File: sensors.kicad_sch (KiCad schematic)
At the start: 55 parts, among them IC1 TCA9548ARGERQ1, IC2 SGP40-D-R4, IC3 SGP40-D-R4, IC4 SGP40-D-R4, IC6 SGP40-D-R4, U3 BMP581, U4 BMP581, U5 BMP581, U6 BMP581

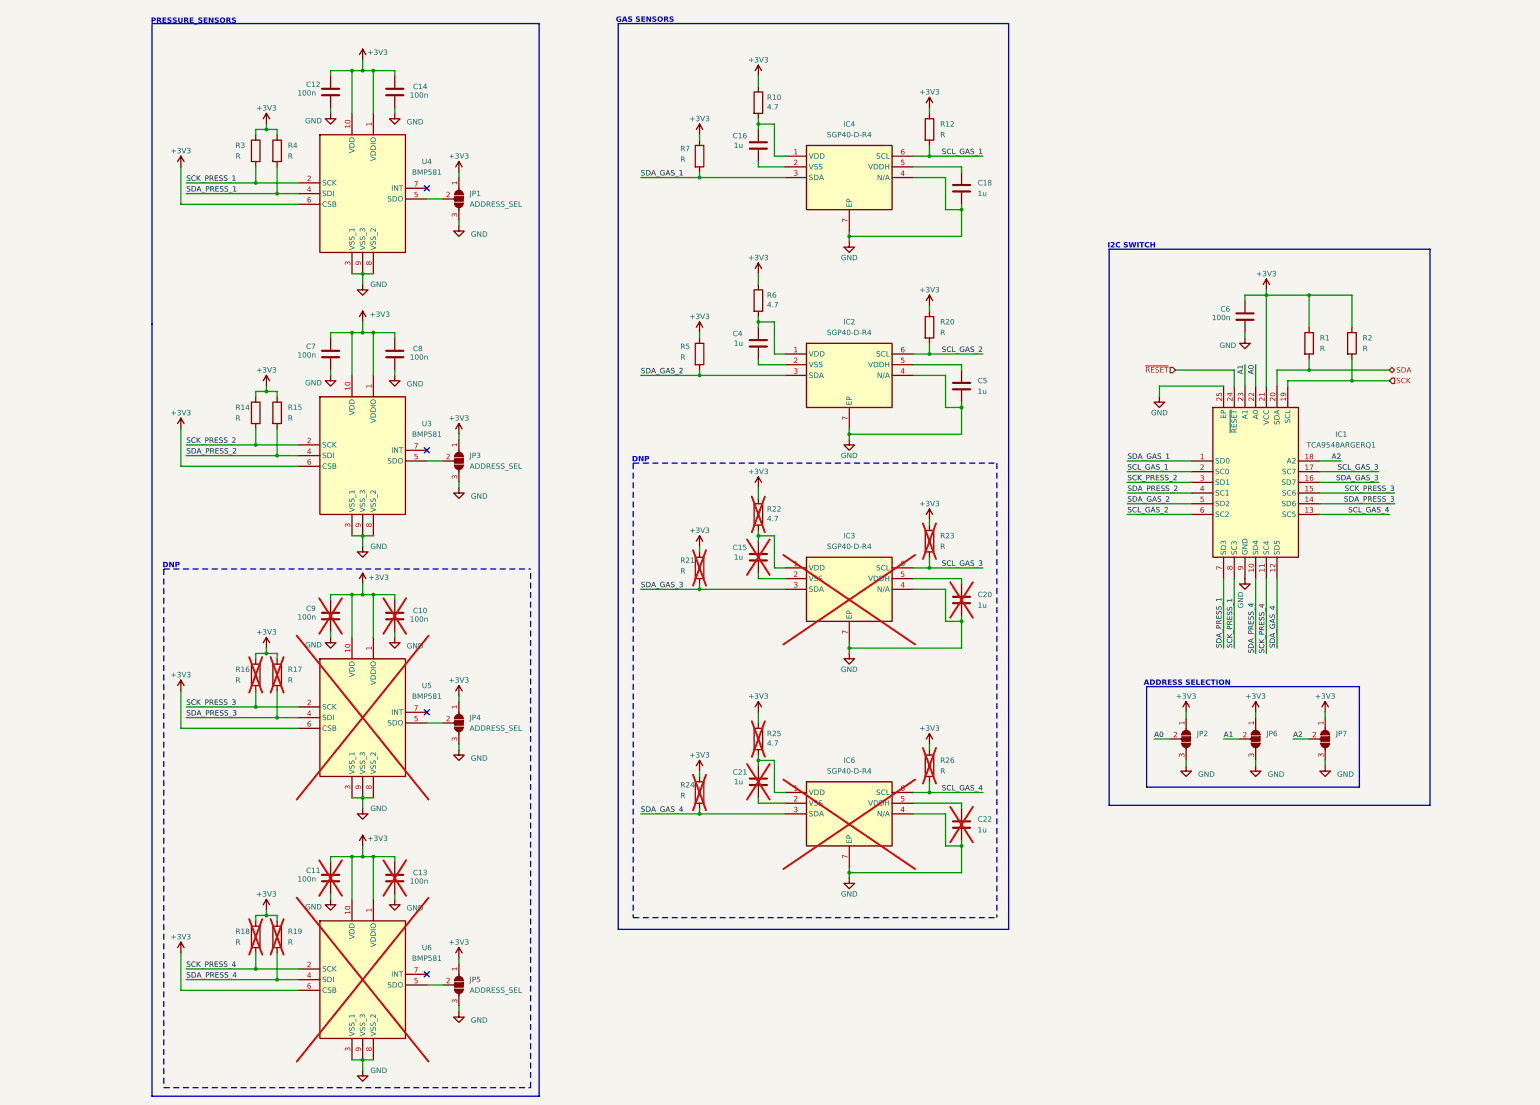
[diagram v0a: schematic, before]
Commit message: fix: 4 channels i2c switch
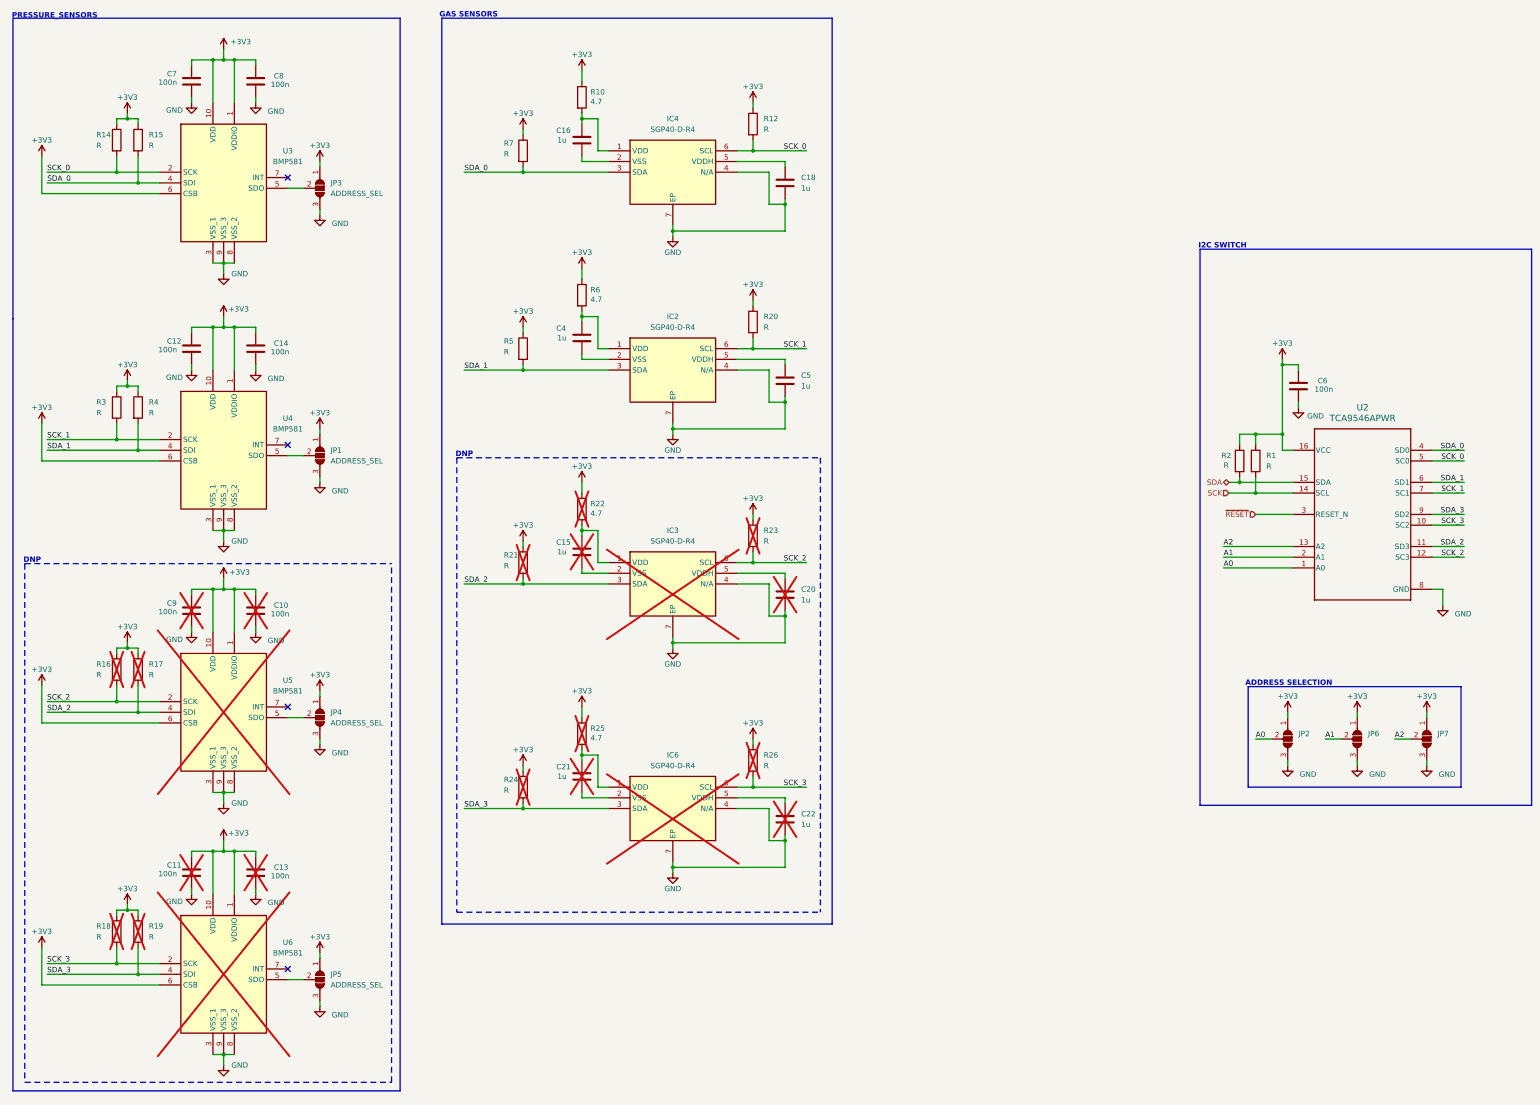
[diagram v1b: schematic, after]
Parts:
- removed IC1: TCA9548ARGERQ1, Local:QFN50P400X400X100-25N-D, symbol TCA:TCA9548ARGERQ1
- added U2: TCA9546APWR, Local:PW0016A-IPC_A, symbol TCA4CH:TCA9546APWR
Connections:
- net SCL_GAS_1 is gone; now on net SCK_0: IC4.6 (SCL), R12.2
- net SCL_GAS_2 is gone; now on net SCK_1: IC2.6 (SCL), R20.2
- net SCL_GAS_3 is gone; now on net SCK_2: IC3.6 (SCL), R23.2
- net SCL_GAS_4 is gone; now on net SCK_3: IC6.6 (SCL), R26.2
- net SDA_PRESS_1 is gone; now on net SDA_1: R4.2, U4.4 (SDI)
- net SDA_PRESS_2 is gone; now on net SDA_0: R15.2, U3.4 (SDI)
- net SDA_PRESS_3 is gone; now on net SDA_2: R17.2, U5.4 (SDI)
- net SDA_PRESS_4 is gone; now on net SDA_3: R19.2, U6.4 (SDI)
- net +3V3: now also U2.16 (VCC)
- net A0: now also U2.1 (A0)
- net A1: now also U2.2 (A1)
- net A2: now also U2.13 (A2)
- net GND: now also U2.8 (GND)
- net SCK: now also R1.2, U2.14 (SCL); no longer R2.2
- net SDA: now also R2.2, U2.15 (SDA); no longer R1.2
- net ~{RESET}: now also U2.3 (RESET_N)
- net SCK_PRESS_1 renamed SCK_1
- net SCK_1: now also U2.7 (SC1)
- net SCK_PRESS_2 renamed SCK_0
- net SCK_0: now also U2.5 (SC0)
- net SCK_PRESS_3 renamed SCK_2
- net SCK_2: now also U2.12 (SC3)
- net SCK_PRESS_4 renamed SCK_3
- net SCK_3: now also U2.10 (SC2)
- net SDA_GAS_1 renamed SDA_0
- net SDA_0: now also U2.4 (SD0)
- net SDA_GAS_2 renamed SDA_1
- net SDA_1: now also U2.6 (SD1)
- net SDA_GAS_3 renamed SDA_2
- net SDA_2: now also U2.11 (SD3)
- net SDA_GAS_4 renamed SDA_3
- net SDA_3: now also U2.9 (SD2)
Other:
- moved on the sheet: C10, C11, C12, C13, C14, C15, C16, C18, C20, C21, C22, C4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

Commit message: feat: add RH sensor
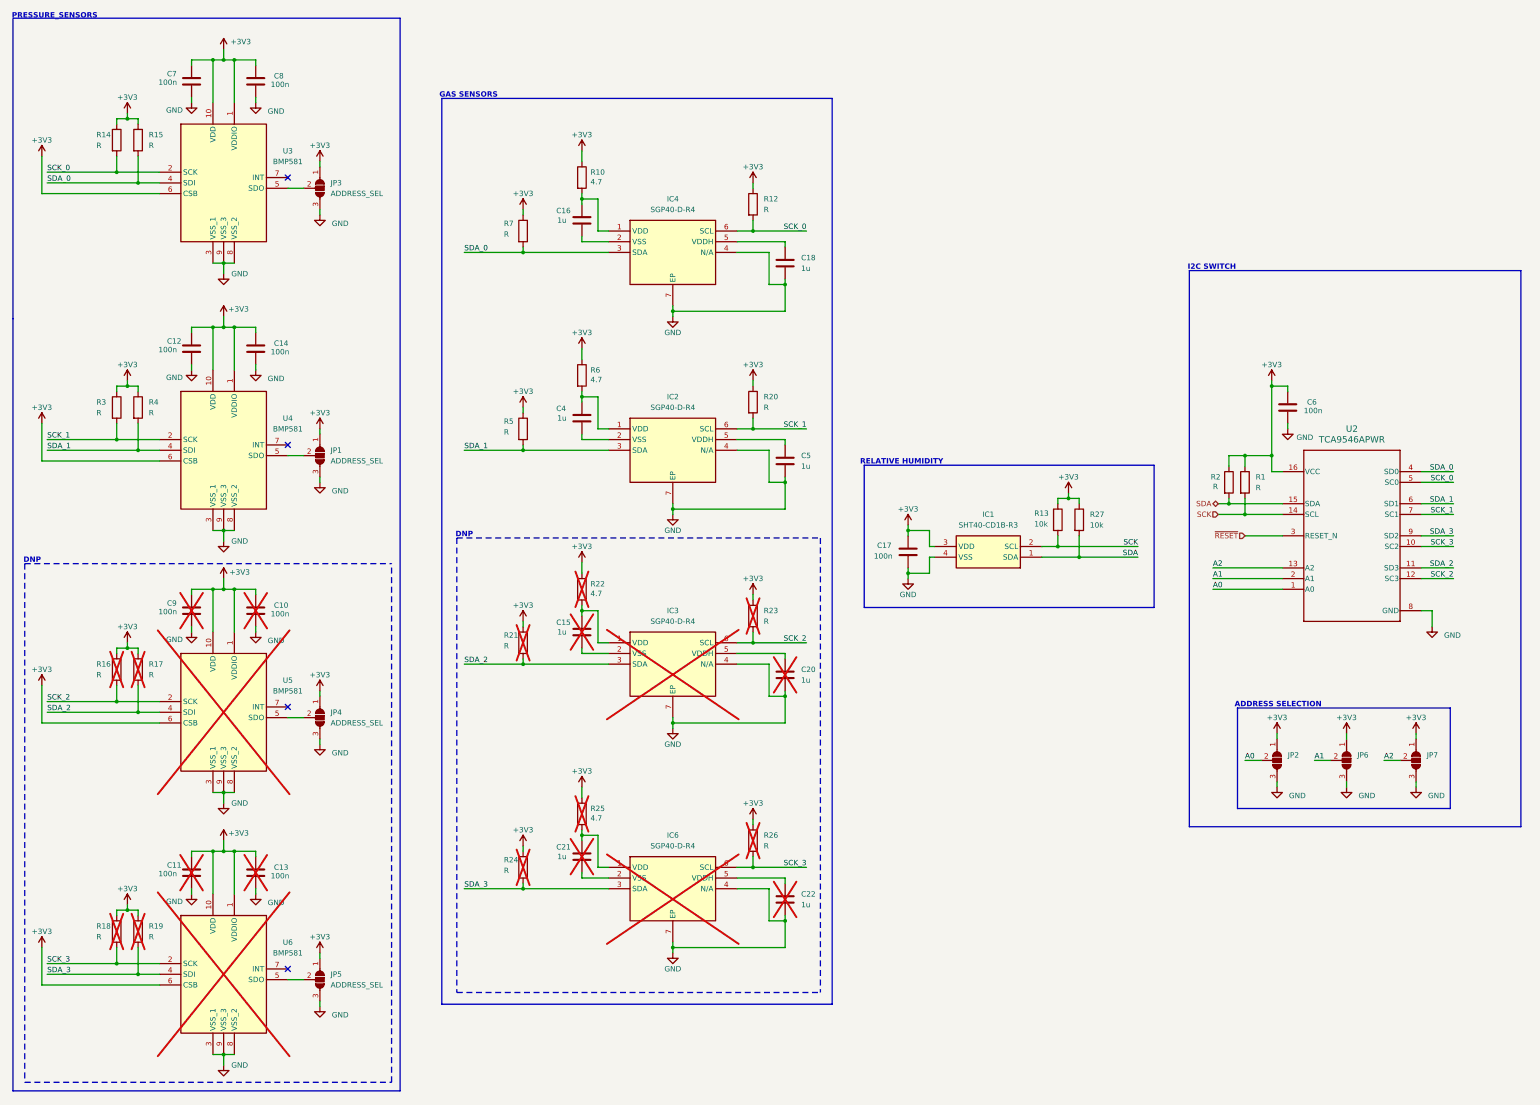
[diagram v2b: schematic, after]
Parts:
- added C17: 100n, Capacitor_SMD:C_0603_1608Metric, symbol Device:C
- added IC1: SHT40-CD1B-R3, Local:SHT40CD1BR3, symbol sht40:SHT40-CD1B-R3
- added R13, R27: 10k, Resistor_SMD:R_0603_1608Metric, symbol Device:R
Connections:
- net +3V3: now also C17.1, IC1.3 (VDD), R13.1, R27.1
- net GND: now also C17.2, IC1.4 (VSS)
- net SCK: now also IC1.2 (SCL), R13.2
- net SDA: now also IC1.1 (SDA), R27.2
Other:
- note added: "RELATIVE HUMIDITY"
- moved on the sheet: C15, C16, C18, C20, C21, C22, C4, C5, C6, IC2, IC3, IC4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

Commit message: fix: unused i2c pullups
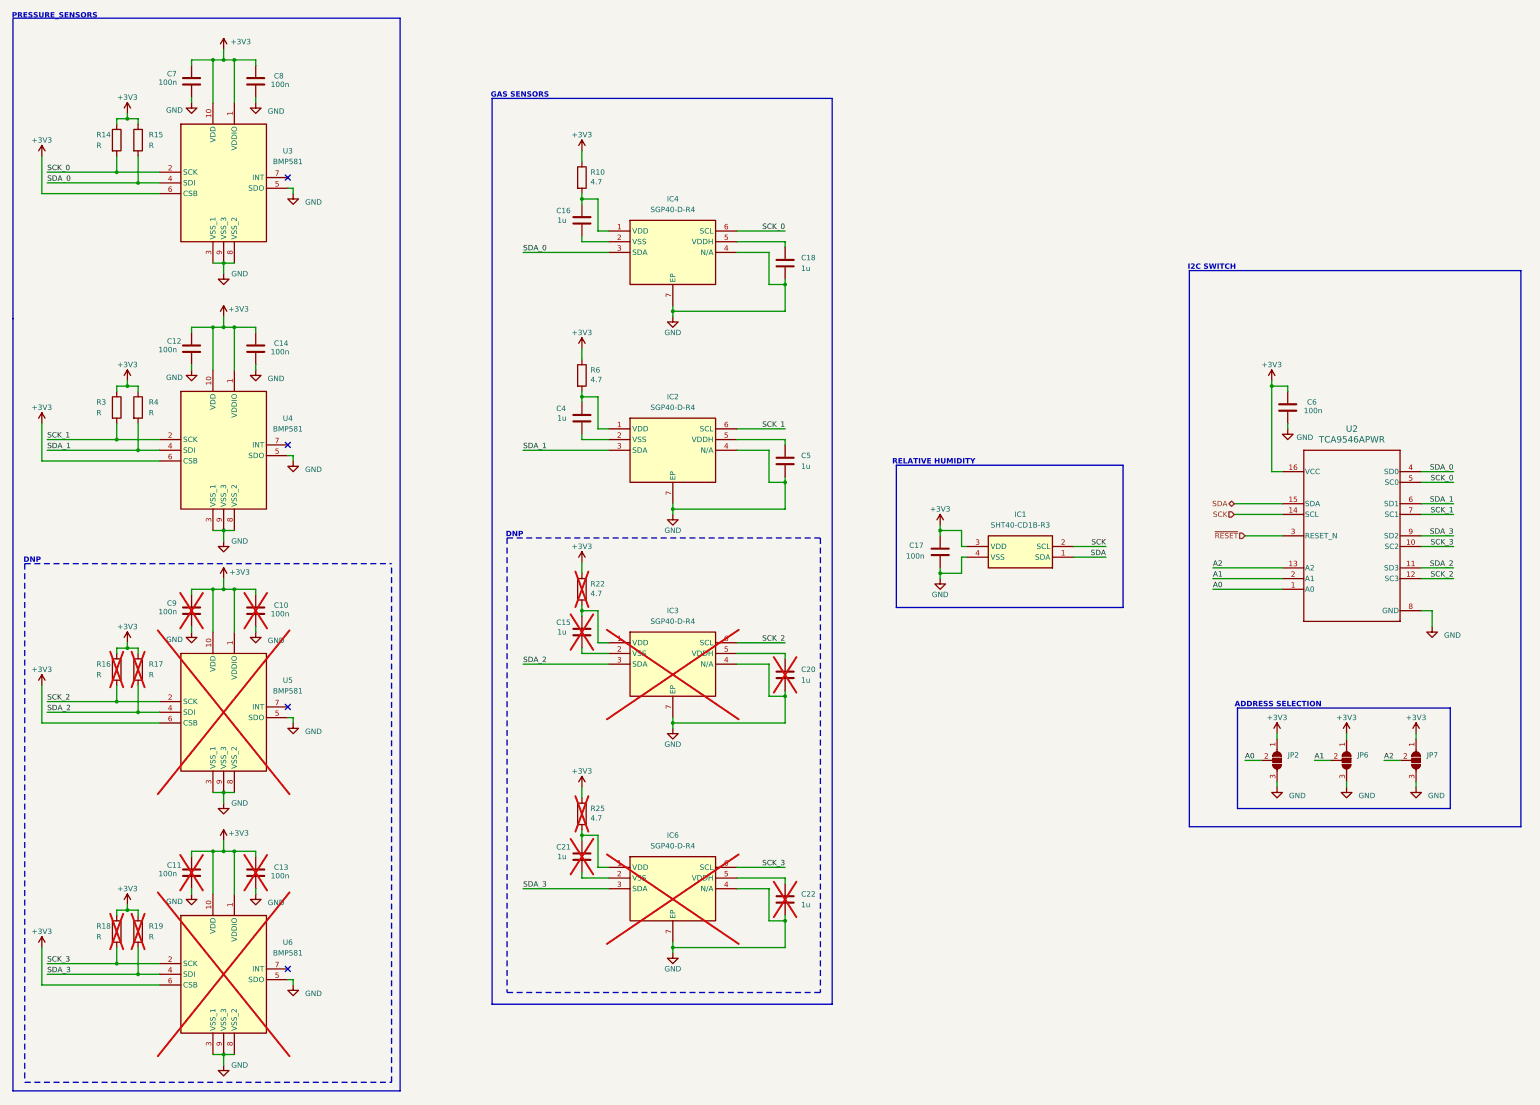
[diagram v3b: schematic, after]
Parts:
- removed JP1, JP3, JP4, JP5: ADDRESS_SEL, Jumper:SolderJumper-3_P1.3mm_Open_RoundedPad1.0x1.5mm, symbol Jumper:SolderJumper_3_Open
- removed R1, R12, R2, R20, R21, R23, R24, R26, R5, R7: R, Resistor_SMD:R_0603_1608Metric, symbol Device:R
- removed R13, R27: 10k, Resistor_SMD:R_0603_1608Metric, symbol Device:R
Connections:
- net GND: now also U3.5 (SDO), U4.5 (SDO), U5.5 (SDO), U6.5 (SDO)
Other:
- moved on the sheet: C17, IC1

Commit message: fix: dnp in opposite edges
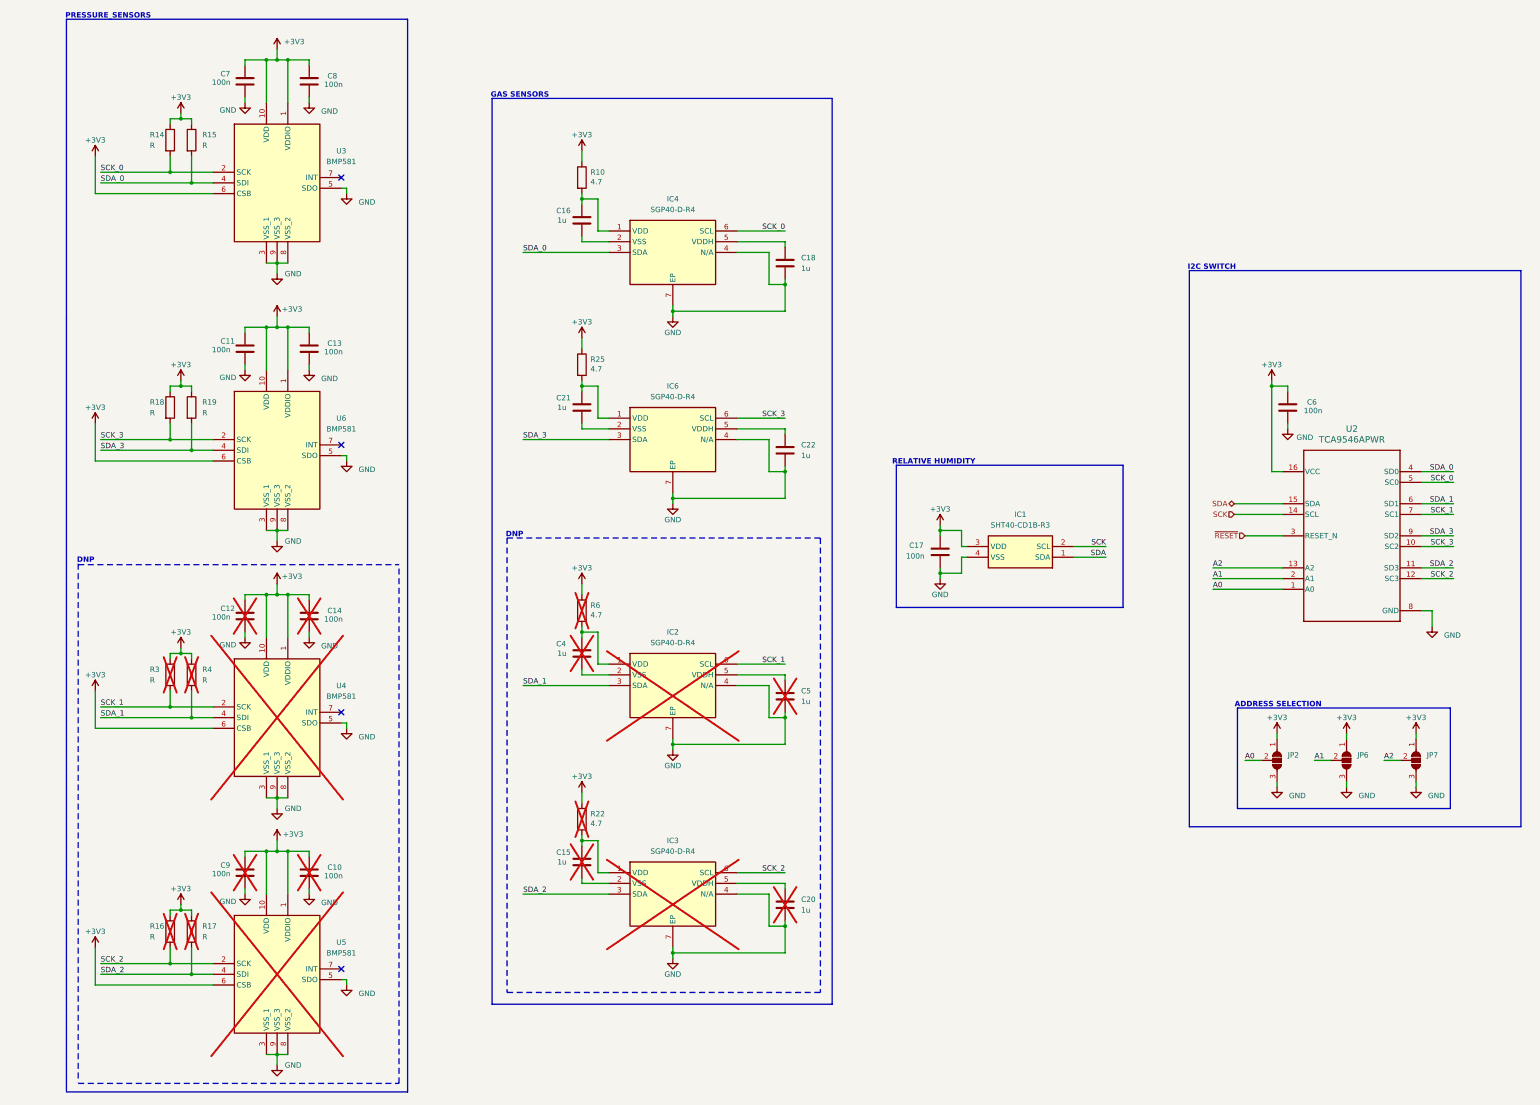
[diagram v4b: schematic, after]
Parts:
- C11, C13, C21, C22, IC6, R18, R19, R25, U6: now fitted; now in the parts list
- C12, C14, C4, C5, IC2, R3, R4, R6, U4: now not fitted; now left out of the parts list
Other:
- moved on the sheet: C10, C15, C20, C7, C8, C9, IC3, R14, R15, R16, R17, R22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
